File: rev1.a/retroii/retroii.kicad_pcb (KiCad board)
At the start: 4 copper layers, 362 x 215.9 mm, 295 parts, among them CON1 SD_Card_SPI, J1 VGA, J10 BARREL_JACK, J11 Conn_02x10, J12 Peripheral Slot 0, J13 74LS74, J14 Game_IO_Socket, J15 Peripheral Slot 4, J16 Peripheral Slot 1, J17 Peripheral Slot 5, J18 Peripheral Slot 2, J19 Peripheral Slot 6, J2 Joystick 1, J20 Peripheral Slot 3, J21 Peripheral Slot 7, J22 Conn_01x09, J23 Conn_01x02, J24 Headphone, J3 Joystick 2, J4 PC Port 1, J5 PC Port 2, J6 Edge mounted connector, J7 Cassette In, J8 Cassette Out, J9 Speaker Jack, K1 PS2_KEYBOARD, K13 LM741, P1 PROP_PLUG, P2 PROP_PLUG, Q4 MPSA13, Q5 2N3904, SW1 SW_PUSH_SAFE, SW2 SPST2, SW3 SAVE, SW4 LOAD, SW5 SW_PUSH_SAFE, SW6 RESET, SW7 MISC1, SW8 MISC2, U1 74LS00, U10 74LS08, U11 LM2576-12, U12 LM2576-5, U13 LM2576-12, U14 LM2576-3.3, U15 LM2576-5, U16 Prop_P8X32A, U17 24LC256_EEPROM, U18 74LS04, U3 74LS11, U4 Prop_P8X32A, U5 24LC256_EEPROM, U6 AT28C256_EEPROM, U8 IDT7008_Dual_Port_RAM, U9 74LS32, Y1 5MHz 20pf, Y2 ECS-2100X-1MHZ, Y3 5MHz 20pf

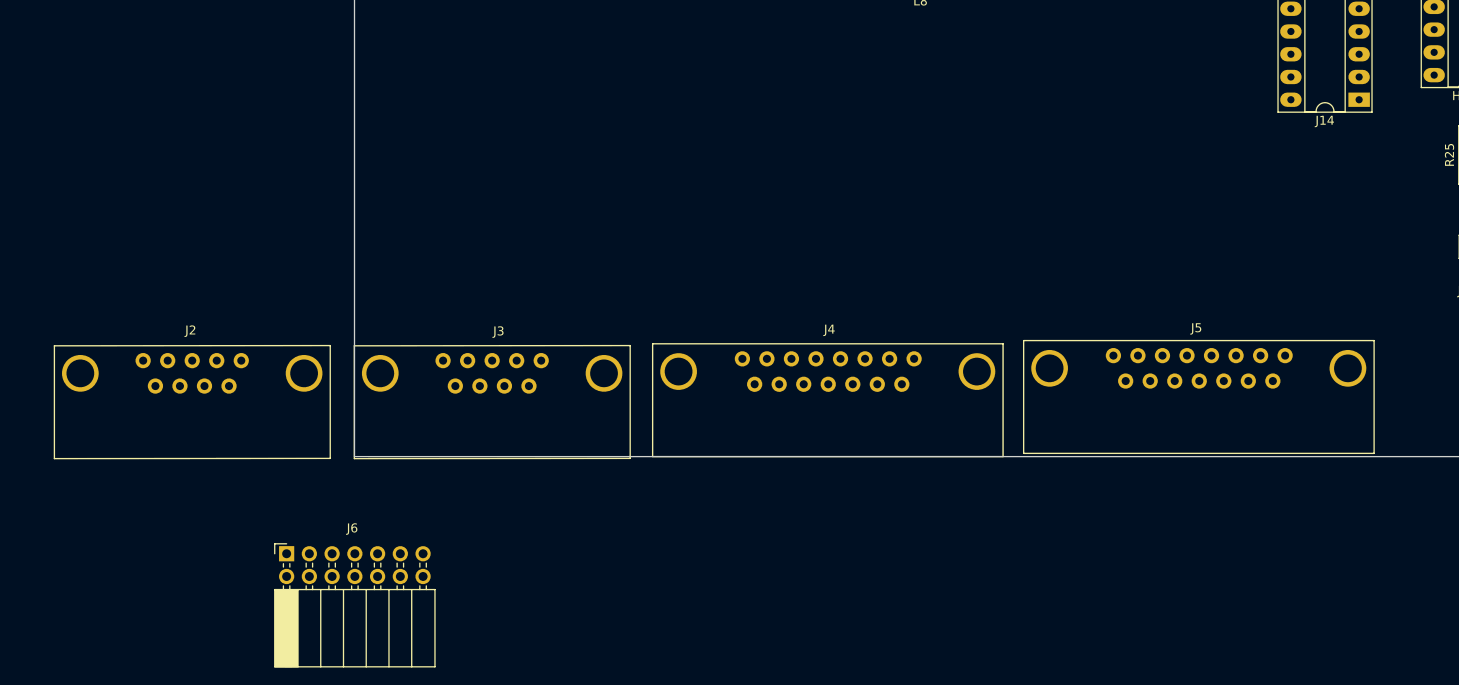
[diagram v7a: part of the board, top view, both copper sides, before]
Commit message: replaced db9/db15 connectors with stacked versions
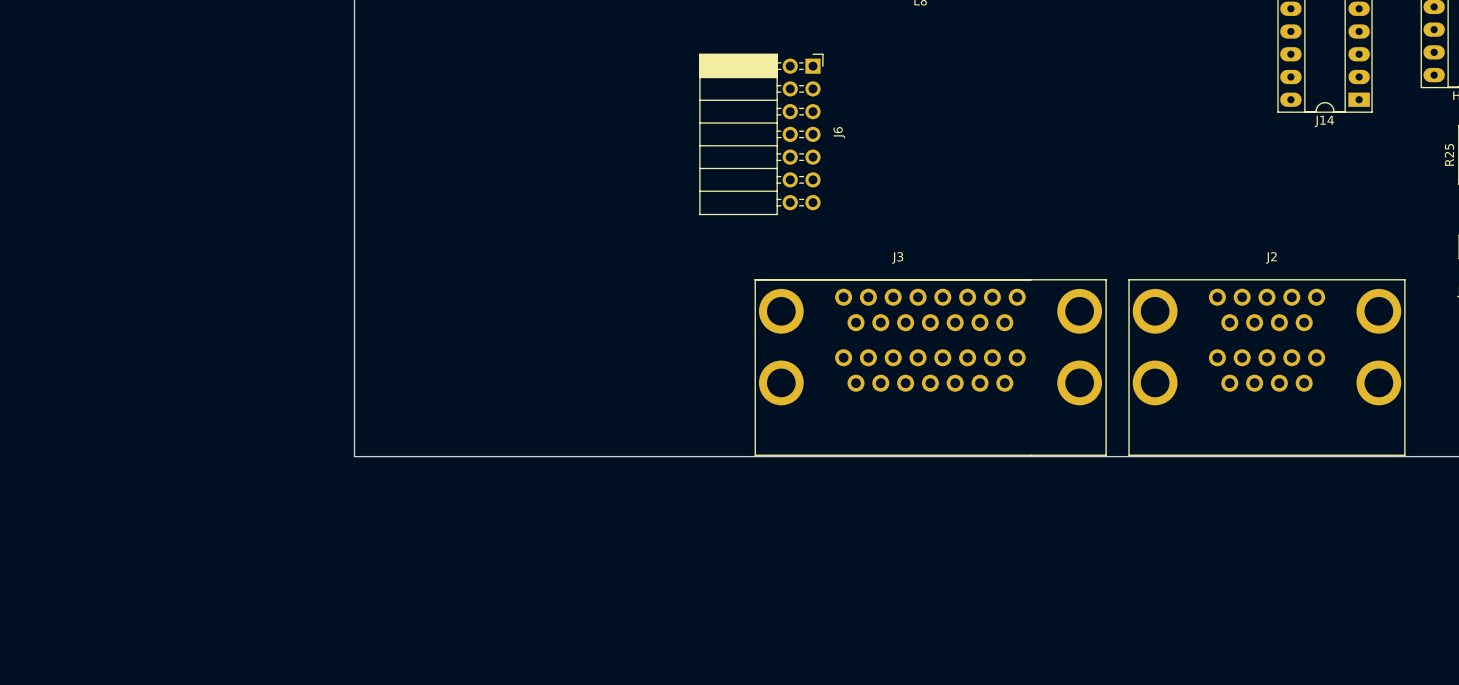
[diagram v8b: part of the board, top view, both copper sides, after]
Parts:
- removed J4: PC Port 1, retroii_footprints:Amphenol_DSUB9_D15S33E4GV00LF
- removed J5: PC Port 2, retroii_footprints:Amphenol_DSUB9_D15S33E4GV00LF
- J2: value Joystick 1 -> DB9_Female_Stacked; footprint retroii_footprints:Amphenol_DSUB9_D09S33E6GV00LF -> retroii_footprints:Amphenol_L17H2220131
- J3: value Joystick 2 -> DB15_Female_Stacked; footprint retroii_footprints:Amphenol_DSUB9_D09S33E6GV00LF -> retroii_footprints:Amphenol_L17H2440131
- moved J2 102.8 mm to (292.0, 350.2), turned to 0 degrees
- moved J6 80.1 mm to (246.2, 322.2), turned to 0 degrees
- moved J3 28.1 mm to (250.2, 350.2), turned to 0 degrees
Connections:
- J2 pad 1: /Serial_IO_Audio/PB1 -> Net-(J2-Pad1)
- J2 pad 5: /Serial_IO_Audio/PDL0 -> /Serial_IO_Audio/PDL2
- J2 pad 7: /Serial_IO_Audio/PB0 -> /Serial_IO_Audio/PB2
- J2 pad 8: /Serial_IO_Audio/PDL1 -> /Serial_IO_Audio/PDL3
- J3 pad 1: Net-(J3-Pad1) -> /Address_Decoding/+5V
- J3 pad 2: /Address_Decoding/+5V -> /Serial_IO_Audio/PB2
- J3 pad 3: GND -> /Serial_IO_Audio/PDL2
- J3 pad 4: Net-(J3-Pad4) -> GND
- J3 pad 5: /Serial_IO_Audio/PDL2 -> GND
- J3 pad 6: Net-(J3-Pad6) -> /Serial_IO_Audio/PDL3
- J3 pad 7: /Serial_IO_Audio/PB2 -> Net-(J3-Pad7)
- J3 pad 8: /Serial_IO_Audio/PDL3 -> /Address_Decoding/+5V
- J3 pad 9: Net-(J3-Pad9) -> /Address_Decoding/+5V
- JP10 pad 1: Net-(J2-Pad4) -> Net-(J2-Pad13)
- JP11 pad 1: Net-(J2-Pad6) -> Net-(J2-Pad15)
- JP12 pad 1: Net-(J4-Pad13) -> Net-(J3-Pad28)
- JP13 pad 1: Net-(J4-Pad11) -> Net-(J3-Pad26)
- JP14 pad 1: Net-(J4-Pad10) -> Net-(J3-Pad25)
- JP9 pad 1: Net-(J2-Pad9) -> Net-(J2-Pad18)
